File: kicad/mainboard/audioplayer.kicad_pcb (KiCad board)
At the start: 4 copper layers, 100.3 x 99.7 mm, 131 parts, among them J1 Micro_SD_Card, J2 USB_B, J3 L, J4 R, J5 LiPo, Q1 DMN2020LSN, Q2 BC847, SW1 VOL-, SW2 VOL+, SW3 RIGHT, SW4 LEFT, SW5 MID, U1 RC-552, U10 PC817, U11 LMC555xM, U12 TPS63001, U2 UMH4NTN, U3 ESP-WROOM32, U4 CP2102N-A02-GQFN24, U5 MCP73831-2-OT, U6 PAM8408, U7 VS1053b, U8 NCP115, U9 MT3608, Y1 12.288MHz

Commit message: board layout finalization
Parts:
- added R29: 2.7k, Resistor_SMD:R_0603_1608Metric, F.Cu at (113.3, 67.8)
- C10, C15, C2, C23, C24: value 1u -> 1u 10V; footprint Capacitor_SMD:C_0603_1608Metric -> Capacitor_SMD:C_0805_2012Metric
- C16: footprint Capacitor_SMD:C_0603_1608Metric -> Capacitor_SMD:C_0805_2012Metric
- C21, C26, C28, C3: value 22u -> 22u 10V; footprint Capacitor_SMD:C_1206_3216Metric -> Capacitor_SMD:C_1210_3225Metric
- C22: footprint Capacitor_SMD:C_1206_3216Metric -> Capacitor_SMD:C_1210_3225Metric
- L1, L2, L3, L4: value L_Core_Ferrite_Small -> 600
- L5: value 10u -> 22u; footprint Inductor_SMD:L_7.3x7.3_H4.5 -> Inductor_SMD:L_Taiyo-Yuden_NR-60xx
- Q1: footprint Package_TO_SOT_SMD:SOT-23 -> Package_TO_SOT_SMD:SC-59
- R30: renamed from R29; value 5.6k -> 2.7k
- R4: footprint Resistor_SMD:R_0603_1608Metric -> Resistor_SMD:R_1206_3216Metric
- U11: footprint Package_SO:SOIC-8_3.9x4.9mm_P1.27mm -> Package_SO:VSSOP-8_3.0x3.0mm_P0.65mm
- moved L3 2.63 mm to (111.0, 46.0)
- moved L4 2.24 mm to (108.6, 46.0)
- moved C8 1.98 mm to (105.9, 46.9)
- moved C6 1.97 mm to (103.6, 61.5)
- moved C9 1.94 mm to (105.8, 45.1)
- moved C5 1.65 mm to (103.6, 63.4)
- moved TP8 0.97 mm to (143.9, 45.3)
- moved R4 0.95 mm to (127.5, 44.7)
- moved TP9 0.65 mm to (128.1, 48.6)
- moved C25 0.60 mm to (121.0, 56.7)
- moved C3 0.58 mm to (140.7, 42.7)
- moved C26 0.55 mm to (132.1, 48.6)
- moved TP1 0.53 mm to (97.2, 53.8)
- moved C28 0.45 mm to (132.1, 56.3)
- moved C1 0.32 mm to (69.5, 34.2)
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- renumbered R30 to R31, R31 to R32, R32 to R33, R33 to R34, R34 to R35, R35 to R36
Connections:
- R30 pad 1: GND -> Net-(R29-Pad2)
- R30 pad 2: Net-(R27-Pad1) -> GND
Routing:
- net Net-(U2-Pad1): track 41.9 -> 55.6 mm
- net GND: track 234.6 -> 223.5 mm, vias 62 -> 57
- net Net-(JP2-Pad3): track 59.8 -> 70.8 mm
- net PWR_DOWN: track 72.0 -> 81.4 mm
- net MP3_XCS: track 20.2 -> 28.1 mm
- net PWR_UP: track 87.1 -> 94.1 mm, vias 2 -> 3
- net Net-(JP1-Pad3): track 68.6 -> 74.9 mm, vias 4 -> 2
- net AMP_EN: track 37.4 -> 43.5 mm
- net /RFID_RST: track 69.1 -> 74.7 mm
- net /RFID_CS: track 63.2 -> 68.0 mm
- net +3V3: track 201.2 -> 196.5 mm, vias 20 -> 16
- net Net-(Q2-Pad3): track 5.30 -> 9.86 mm
- net BATT: track 123.1 -> 119.5 mm, vias 10 -> 9
- net Net-(C5-Pad1): track 68.7 -> 65.2 mm, vias 0 -> 2
- net /SCK: track 104.3 -> 107.4 mm
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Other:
- net class Default: trace_width 0.25 -> 0.4
- rule pad_to_mask_clearance: 0 -> 0.05
- rule via_min_drill: 0.3 -> 0.2
- rule via_min_size: 0.4 -> 0.45

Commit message: board polish
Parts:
- moved TP7 13.4 mm to (124.2, 59.6)
- moved C22 9.81 mm to (110.9, 62.2), turned to 270 degrees
- moved R30 6.71 mm to (108.2, 67.1)
- moved R28 3.34 mm to (113.0, 68.0)
- moved R27 3.34 mm to (114.6, 68.0)
- moved C25 2.89 mm to (118.2, 56.2)
- moved R29 2.88 mm to (110.6, 68.8), turned to 180 degrees
- moved L5 0.70 mm to (123.9, 65.2)
- moved C24 0.21 mm to (112.5, 56.4)
- moved C23 0.08 mm to (112.5, 51.5)
- moved L1 0.06 mm to (108.2, 61.6)
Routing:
- net BATT: track 119.5 -> 138.1 mm, vias 9 -> 15
- net Net-(R27-Pad1): track 5.41 -> 0.00 mm
- net GND: track 223.5 -> 219.0 mm, vias 57 -> 70
- net EN: track 86.9 -> 89.6 mm
- net Net-(R29-Pad2): track 1.60 -> 0.00 mm
- net Net-(D9-Pad2): track 9.89 -> 8.66 mm
- net +6V: track 37.8 -> 38.5 mm, vias 2 -> 0

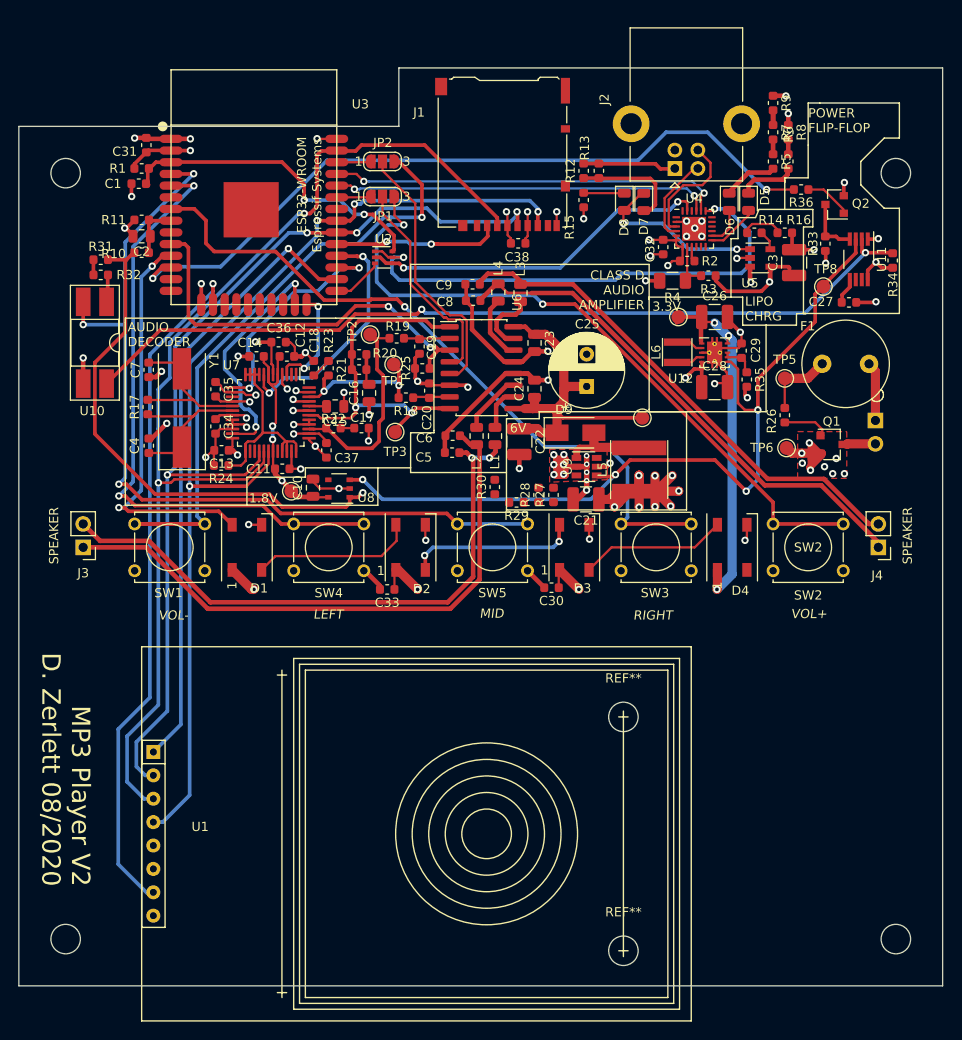
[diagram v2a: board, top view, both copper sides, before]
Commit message: use zener diode array
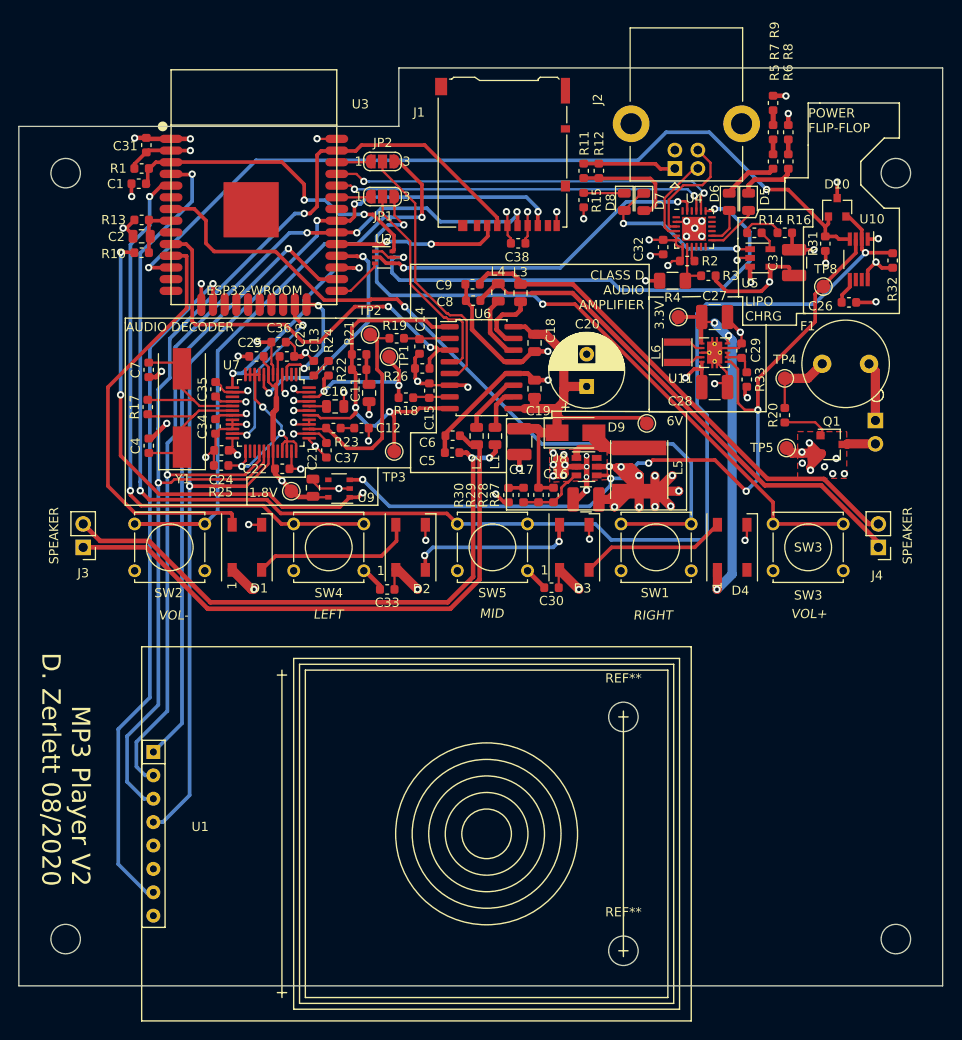
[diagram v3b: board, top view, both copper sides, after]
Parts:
- removed the C20 at (101.1, 56.6)
- removed the C21 at (118.1, 68.5)
- removed Q2: BC847, Package_TO_SOT_SMD:SOT-23
- removed the R25 at (100.3, 54.2)
- removed the R31 at (65.4, 42.4)
- removed the R32 at (65.4, 44.1)
- removed R36: 10k, Resistor_SMD:R_0603_1608Metric
- removed the U10 at (64.8, 51.4)
- added C15: 4.7n, Capacitor_SMD:C_0603_1608Metric, F.Cu at (101.1, 56.6)
- added C16: 22u, Capacitor_SMD:C_1210_3225Metric, F.Cu at (118.1, 68.5)
- added D10: 3.3V, Package_TO_SOT_SMD:SOT-23, F.Cu at (145.4, 36.7)
- added R26: 10k, Resistor_SMD:R_0603_1608Metric, F.Cu at (100.3, 54.2)
- C10: renamed from C15; value 1u 10V -> 1u
- C18: renamed from C23; value 1u 10V -> 1u
- C19: renamed from C24; value 1u 10V -> 1u
- C2: value 1u 10V -> 1u
- C21: renamed from C10; value 1u 10V -> 1u
- C27: renamed from C26; value 22u 10V -> 22u
- C28, C3: value 22u 10V -> 22u
- moved TP3 2.11 mm to (97.3, 63.2)
- moved R30 1.73 mm to (109.7, 68.0), turned to 270 degrees
- moved R29 1.11 mm to (111.3, 68.0), turned to 90 degrees
- moved TP1 0.97 mm to (96.7, 52.9)
- moved TP6 0.78 mm to (124.7, 60.2)
- renumbered C16 to C11, C17 to C12, C18 to C13, C19 to C14, C22 to C17, C25 to C20, C11 to C22, C12 to C23, C13 to C24, C14 to C25, C27 to C26, R12 to R11, R13 to R12, R11 to R13, R26 to R20, R20 to R21, R21 to R22, R22 to R23, R23 to R24, R24 to R25, R33 to R31, R34 to R32, R35 to R33, SW3 to SW1, SW1 to SW2, SW2 to SW3, TP5 to TP4, TP6 to TP5, TP7 to TP6, TP4 to TP7, U11 to U10, U12 to U11, U9 to U8, U8 to U9
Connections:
- net /RFID_CS renamed RFID_CS
- net /RFID_RST renamed RFID_RST
- R31 pad 1: Net-(Q2-Pad3) -> PWR_DOWN
- R32 pad 1: Net-(R34-Pad1) -> PWR_UP
- U10 pad 2: Net-(R34-Pad1) -> PWR_UP
- U10 pad 4: Net-(Q2-Pad3) -> PWR_DOWN
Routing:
- net Net-(R34-Pad1): track 94.3 -> 0.00 mm, vias 2 -> 0
- net PWR_UP: track 94.1 -> 156.8 mm
- net PWR_DOWN: track 81.4 -> 91.4 mm
- net Net-(Q2-Pad3): track 9.86 -> 0.00 mm
- net MP3_XCS: track 28.1 -> 18.7 mm
- net +6V: track 38.5 -> 46.3 mm
- net Net-(R27-Pad1): track 0.00 -> 7.47 mm
- net Net-(SW1-Pad1): track 77.3 -> 84.3 mm
- net Net-(Q2-Pad1): track 5.30 -> 0.00 mm
- net Net-(SW4-Pad2): track 67.4 -> 62.7 mm
- net WS2812: track 43.7 -> 47.2 mm, vias 2 -> 0
- net Net-(R21-Pad2): track 42.0 -> 44.9 mm
- net BATT: track 138.1 -> 140.6 mm, vias 15 -> 18
- net +1V8: track 35.0 -> 32.5 mm, vias 4 -> 2
- net Net-(R32-Pad1): track 2.48 -> 0.00 mm
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- added copper zone on In2.Cu, net +1V8

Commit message: new board v1
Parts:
- removed ?: MountingHole_3.2mm_M3, MountingHole:MountingHole_3.2mm_M3
- removed the C30 at (114.4, 78.0)
- removed the C33 at (96.5, 78.2)
- removed the R28 at (113.0, 68.0)
- removed the R29 at (111.3, 68.0)
- removed the REF** at (151.8, 33.0)
- removed the REF** at (61.6, 33.0)
- removed the REF** at (151.8, 116.2)
- added C21: 100n, Capacitor_SMD:C_0603_1608Metric, F.Cu at (98.1, 78.0)
- added C22: 100n, Capacitor_SMD:C_0603_1608Metric, F.Cu at (115.9, 78.1)
- added C23: 100n, Capacitor_SMD:C_0603_1608Metric, F.Cu at (80.5, 78.0)
- added C24: 100n, Capacitor_SMD:C_0603_1608Metric, F.Cu at (133.2, 78.0)
- added R31: 27k, Resistor_SMD:R_0603_1608Metric, F.Cu at (111.8, 67.9)
- added REF**: MountingHole_2.7mm_M2.5_DIN965, MountingHole:MountingHole_2.7mm_M2.5_DIN965, F.Cu at (151.8, 81.4)
- added REF**: MountingHole_2.7mm_M2.5_DIN965, MountingHole:MountingHole_2.7mm_M2.5_DIN965, F.Cu at (61.6, 81.4)
- added REF**: MountingHole_2.7mm_M2.5_DIN965, MountingHole:MountingHole_2.7mm_M2.5_DIN965, F.Cu at (61.6, 116.2)
- added REF**: MountingHole_2.7mm_M2.5_DIN965, MountingHole:MountingHole_2.7mm_M2.5_DIN965, F.Cu at (61.6, 33.0)
- added REF**: MountingHole_2.7mm_M2.5_DIN965, MountingHole:MountingHole_2.7mm_M2.5_DIN965, F.Cu at (151.8, 33.0)
- added REF**: MountingHole_2.7mm_M2.5_DIN965, MountingHole:MountingHole_2.7mm_M2.5_DIN965, F.Cu at (151.8, 116.2)
- added REF**: MountingHole_2.7mm_M2.5_DIN965, MountingHole:MountingHole_2.7mm_M2.5_DIN965, F.Cu at (108.0, 81.4)
- F1: footprint Fuse:Fuseholder_TR5_Littelfuse_No560_No460 -> Fuse:Fuse_Littelfuse_372_D8.50mm
- L6: footprint Inductor_SMD:L_Taiyo-Yuden_NR-30xx -> Inductor_SMD:L_Taiyo-Yuden_NR-60xx
- R3: footprint Resistor_SMD:R_0603_1608Metric -> Resistor_SMD:R_1206_3216Metric
- R30: value 2.7k -> 20k
- TP6: value TestPoint_5V5 -> TestPoint_5V3
- Y1: footprint Crystal:Crystal_SMD_HC49-SD -> audioplayer:Crystal_SMD_ABLS7M
- moved C7 5.39 mm to (75.7, 52.6), turned to 180 degrees
- moved C4 4.37 mm to (74.7, 64.3), turned to 0 degrees
- moved C20 2.91 mm to (116.5, 53.8), turned to 0 degrees
- moved L6 1.58 mm to (126.4, 52.4)
- moved TP9 1.42 mm to (128.4, 47.2)
- moved R27 1.23 mm to (113.3, 67.9)
- moved R3 0.91 mm to (132.1, 44.7)
- moved J1 0.89 mm to (109.0, 30.1)
- moved R17 0.86 mm to (71.4, 58.4)
- moved R30 0.85 mm to (108.8, 67.9), turned to 90 degrees
- moved TP7 0.81 mm to (144.4, 44.7)
- moved C40 0.76 mm to (110.7, 39.9)
- moved Y1 0.45 mm to (74.7, 58.5)
- renumbered C21 to C25, C22 to C26, C23 to C27, C24 to C28, C25 to C29, C26 to C30, C27 to C31, C28 to C32, C29 to C33, C31 to C34, C32 to C35, C34 to C36, C35 to C37, C36 to C38, C37 to C39, C38 to C40, D5 to D1, D6 to D2, D7 to D3, D8 to D4, D1 to D5, D2 to D6, D3 to D7, D4 to D8, R31 to R28, R32 to R29, R33 to R32, TP8 to TP7, TP7 to TP8, U9 to U10, U10 to U9
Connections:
- D5 pad 1: +3V3 -> +6V
- D6 pad 1: +3V3 -> +6V
- D7 pad 1: +3V3 -> +6V
- D8 pad 1: +3V3 -> +6V
- R30 pad 1: Net-(R29-Pad2) -> Net-(R27-Pad1)
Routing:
- net +6V: track 46.3 -> 135.9 mm, vias 0 -> 4
- net +3V3: track 195.4 -> 107.7 mm, vias 16 -> 12
- net GND: track 218.6 -> 244.2 mm
- net Net-(JP1-Pad3): track 74.9 -> 83.9 mm
- net PWR_UP: track 156.8 -> 148.7 mm
- net Net-(C4-Pad2): track 17.8 -> 13.4 mm
- net BATT: track 140.6 -> 144.3 mm
- net Net-(C9-Pad2): track 55.5 -> 58.3 mm
- net Net-(C8-Pad2): track 56.6 -> 59.3 mm
- net Net-(R3-Pad1): track 5.98 -> 8.15 mm
- net Net-(SW1-Pad1): track 84.3 -> 82.4 mm
- net Net-(C7-Pad2): track 17.3 -> 15.5 mm
- net Net-(R29-Pad2): track 1.68 -> 0.00 mm
- net EN: track 89.9 -> 88.2 mm, vias 5 -> 3
- net Net-(R27-Pad1): track 7.47 -> 9.03 mm
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- added copper zone on In2.Cu, net +6V
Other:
- board text added: "MP3 Player V2 REV 1 D. Zerlett 08/2020 für Mika und Linus"
- board text removed: "MP3 Player V2 D. Zerlett 08/2020"
- board text removed: "POWER FLIP-FLOP"

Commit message: new board software first step
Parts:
- added C41: 100n, Capacitor_SMD:C_0603_1608Metric, F.Cu at (145.9, 29.5)
- added D11: US1A, Diode_SMD:D_SMA, F.Cu at (124.6, 60.0)
- added D12: US1A, Diode_SMD:D_SMA, F.Cu at (131.1, 66.0)
- added Q2: SSM3J332R, Package_TO_SOT_SMD:SOT-23, F.Cu at (136.9, 61.3)
- added Q3: BC547, Package_TO_SOT_SMD:SOT-23, F.Cu at (137.4, 51.5)
- added R33: 1k, Resistor_SMD:R_0603_1608Metric, F.Cu at (140.9, 52.8)
- added R34: 10k, Resistor_SMD:R_0603_1608Metric, F.Cu at (140.6, 46.5)
- added R35: 220k, Resistor_SMD:R_0603_1608Metric, F.Cu at (145.9, 27.8)
- J2: moved to B.Cu
- moved TP6 7.45 mm to (117.3, 59.1)
- moved J2 2.54 mm to (130.3, 32.5)
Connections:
- C16 pad 1: BATT -> BATT_SWITCHED
- C21 pad 1: +6V -> +4V
- C22 pad 1: +6V -> +4V
- C23 pad 1: +6V -> +4V
- C24 pad 1: +6V -> +4V
- C32 pad 1: BATT -> BATT_SWITCHED
- D10 pad 1: PWR_DOWN -> Net-(C41-Pad1)
- D5 pad 1: +6V -> +4V
- D6 pad 1: +6V -> +4V
- D7 pad 1: +6V -> +4V
- D8 pad 1: +6V -> +4V
- L5 pad 1: BATT -> BATT_SWITCHED
- R10 pad 2: BATT -> BATT_SWITCHED
- R28 pad 1: PWR_DOWN -> Net-(C41-Pad1)
- R32 pad 2: BATT -> BATT_SWITCHED
- TP7 pad 1: EN -> /EN
- U10 pad 1: BATT -> BATT_SWITCHED
- U10 pad 3: EN -> BATT_SWITCHED
- U11 pad 5: BATT -> BATT_SWITCHED
- U11 pad 6: EN -> Net-(C33-Pad1)
- U8 pad 4: EN -> BATT_SWITCHED
- U8 pad 5: BATT -> BATT_SWITCHED
- U9 pad 3: EN -> /EN
- U9 pad 4: PWR_DOWN -> Net-(C41-Pad1)
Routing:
- net BATT: track 144.3 -> 26.6 mm, vias 18 -> 3
- net BATT_SWITCHED: track 0.00 -> 107.1 mm, vias 0 -> 16
- net +6V: track 135.9 -> 36.6 mm, vias 4 -> 0
- net EN: track 88.2 -> 0.00 mm, vias 3 -> 0
- net +4V: track 0.00 -> 24.7 mm, vias 0 -> 6
- net GND: track 244.2 -> 224.7 mm, vias 69 -> 73
- net Net-(C41-Pad1): track 0.00 -> 17.3 mm
- net Net-(Q2-Pad1): track 0.00 -> 11.5 mm
- net /EN: track 0.00 -> 9.91 mm
- net Net-(C5-Pad1): track 65.2 -> 56.9 mm
- net Net-(C6-Pad1): track 64.7 -> 56.6 mm
- net Net-(Q3-Pad2): track 0.00 -> 4.67 mm
- net Net-(C3-Pad1): track 41.5 -> 44.4 mm, vias 1 -> 2
- net Net-(J2-Pad3): track 12.6 -> 10.6 mm
- net Net-(D9-Pad2): track 10.4 -> 12.2 mm
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- added copper zone on In2.Cu, net +4V
- added copper zone on In2.Cu, net BATT_SWITCHED
- removed copper zone on In2.Cu, net +6V
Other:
- board text added: "MP3 Player V2 REV 2 D. Zerlett 10/2020 für Mika und Linus"
- board text removed: "6V"
- board text removed: "AUDIO DECODER"
- board text removed: "CLASS D AUDIO AMPLIFIER"
- board text removed: "LIPO CHRG"
- board text removed: "MP3 Player V2 REV 1 D. Zerlett 08/2020 für Mika und Linus"
